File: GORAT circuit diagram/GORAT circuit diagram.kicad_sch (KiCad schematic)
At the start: 69 parts, among them J1 AudioJack2, J10 Conn_01x02_Socket, J11 Conn_01x02_Socket, J2 AudioJack2, J3 Conn_01x08_Socket, J4 Conn_01x08_Socket, J5 Conn_01x02_Socket, J6 Barrel_Jack, J7 Conn_01x02_Socket, J8 Conn_01x03_Socket, J9 Conn_01x03_Socket, Q1 J111, SW3 SW_Rotary4x3, SW8 SW_Rotary2x6, U1 OP07CP, U2 TL072ACP, U3 TL072ACP

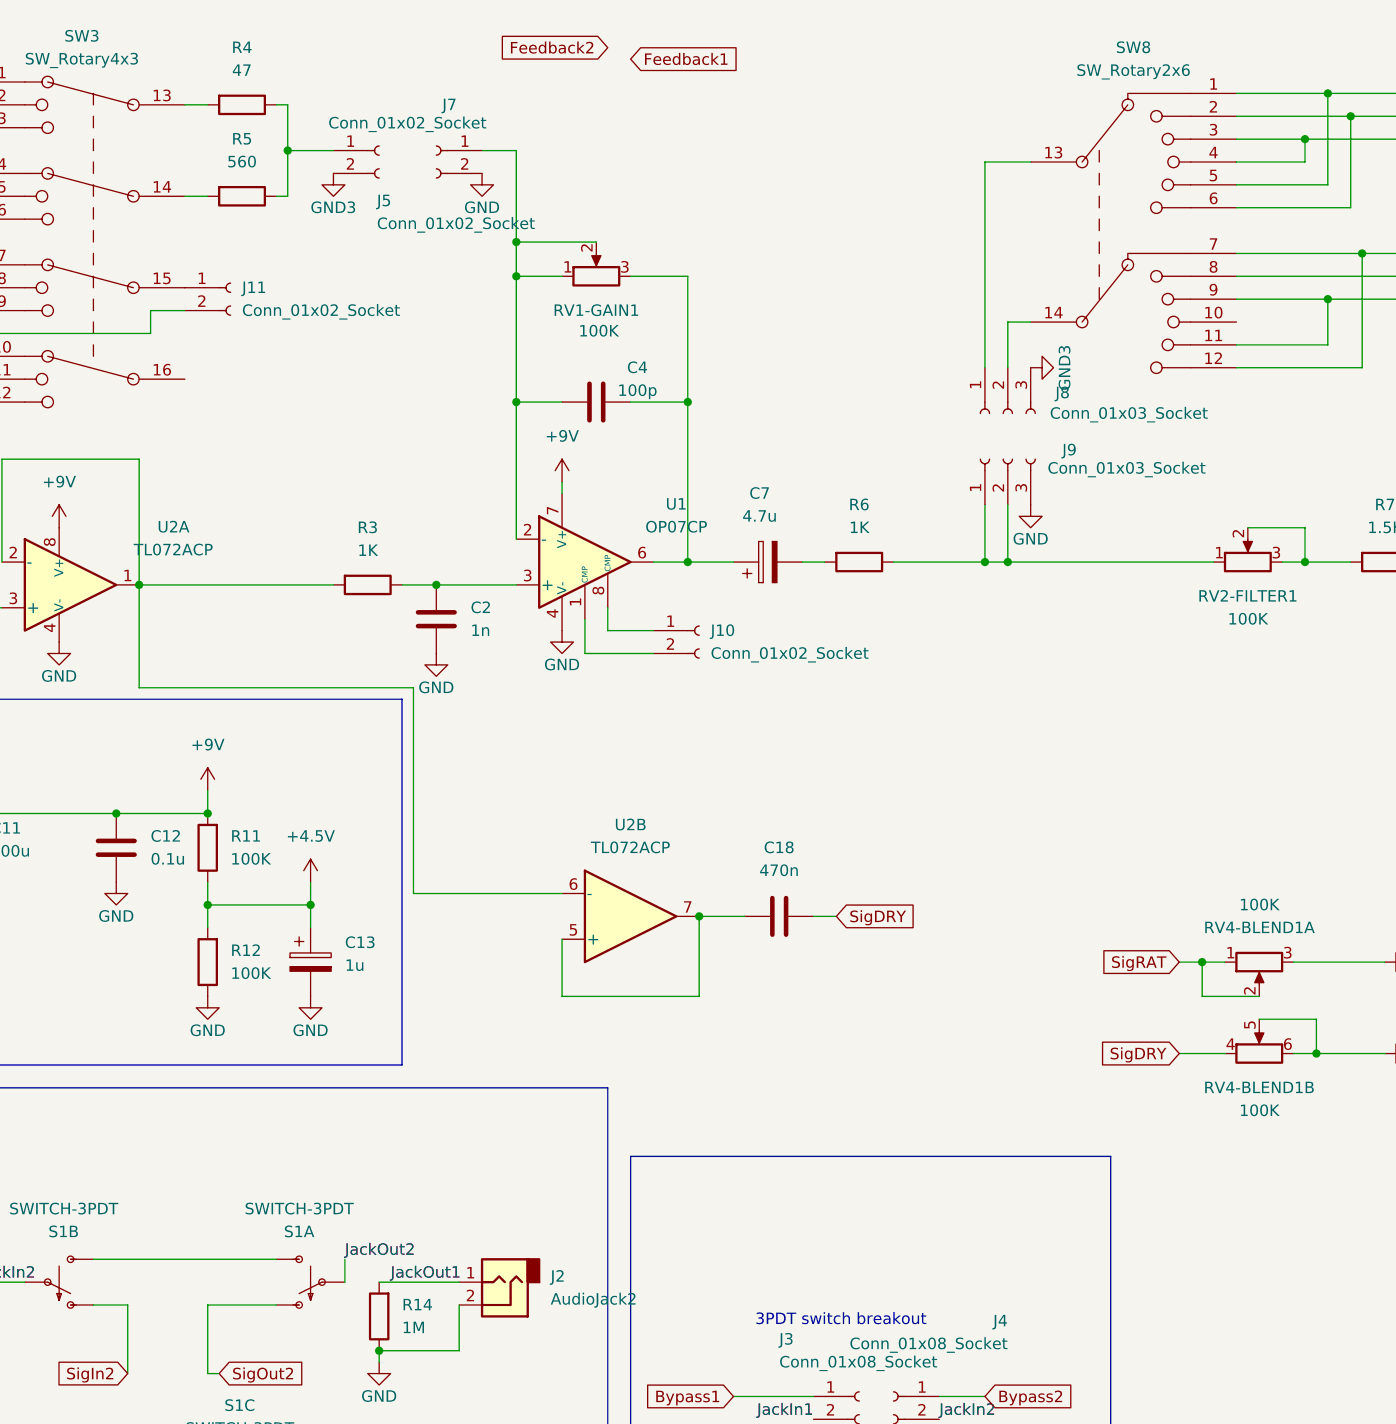
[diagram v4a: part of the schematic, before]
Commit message: Update KiCad PCB, add backups and artwork
Modify GORAT circuit diagram.kicad_pcb: reorder/renumber nets, adjust several pad/net assignments and component positions, and add numerous F.Fab properties (Availability, Check_prices, Description_1, MF, MP, Package, Price, Sim.Type, SnapEDA_Link) for multiple footprints. Remove several old backup ZIPs and add new timestamped backup ZIPs. Add new project assets: GoRAT.csv and artwork/renders (goram-mirror.svg, goram.png, goram.svg, underside.svg). These changes appear to be from a PCB/footprint update and exporting backup/artwork files.
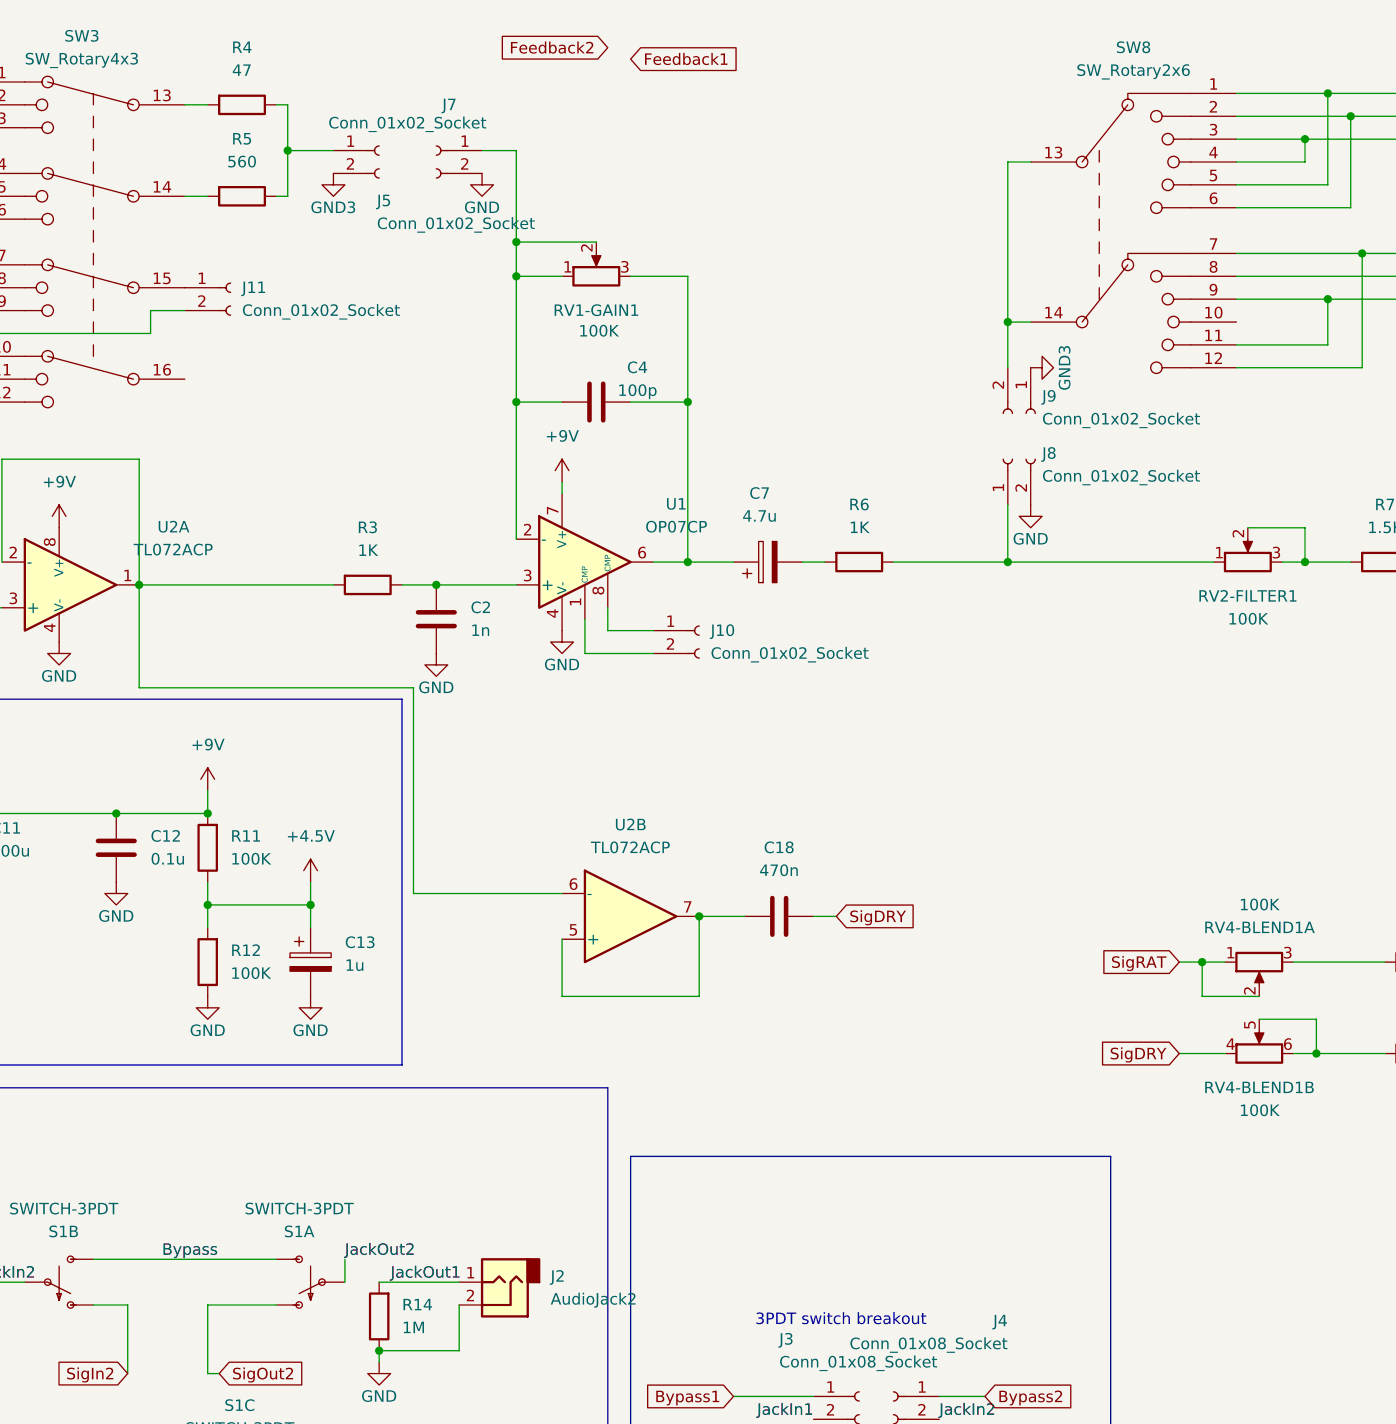
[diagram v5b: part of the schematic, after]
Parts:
- removed J8, J9: Conn_01x03_Socket, Connector_PinHeader_2.54mm:PinHeader_1x03_P2.54mm_Vertical, symbol Connector:Conn_01x03_Socket
- added J8, J9: Conn_01x02_Socket, Connector_PinHeader_2.54mm:PinHeader_1x02_P2.54mm_Vertical, symbol Connector:Conn_01x02_Socket
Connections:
- net GND: now also J8.2 (Pin_2)
- net GND3: now also J9.1 (Pin_1)
- net at SW8.13: now also SW8.14, J9.2 (Pin_2)
- net at R6.1, RV2-FILTER1.1: now also J8.1 (Pin_1)
- net Bypass: now reaches S1.P$3 (S), S1.P$6 (S)

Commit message: Update disc capacitor footprints and BOM
Replace THT disc capacitor footprints with smaller C_Disc_D4.7mm_W2.5mm variants across schematic and PCB (updated 3D model paths, silk/text positions, rotations and UUIDs). Update project metadata: change active board layer in .kicad_prl, set BOM export filename in .kicad_pro, and add generated BOM CSV/XLSX. Add KiCad backup archives and remove autosave/.lck temporary files to keep the repo clean.
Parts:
- C20, C21: footprint Capacitor_THT:C_Disc_D5.1mm_W3.2mm_P5.00mm -> Capacitor_THT:C_Disc_D4.7mm_W2.5mm_P5.00mm
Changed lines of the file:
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@@
 			)
 		)
-		(property "Footprint" "Capacitor_THT:C_Disc_D5.1mm_W3.2mm_P5.00mm"
+		(property "Footprint" "Capacitor_THT:C_Disc_D4.7mm_W2.5mm_P5.00mm"
 			(at 43.18 35.2552 0)
 			(effects
@@
 			)
 		)
-		(property "Footprint" "Capacitor_THT:C_Disc_D5.1mm_W3.2mm_P5.00mm"
+		(property "Footprint" "Capacitor_THT:C_Disc_D4.7mm_W2.5mm_P5.00mm"
 			(at 43.18 23.1648 0)
 			(effects

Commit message: BOM work
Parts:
- added TP1: Input, TestPoint:TestPoint_Pad_D2.0mm, symbol Connector:TestPoint
- added TP2: Pre-gain, TestPoint:TestPoint_Pad_D2.0mm, symbol Connector:TestPoint
- added TP3: Post-gain, TestPoint:TestPoint_Pad_D2.0mm, symbol Connector:TestPoint
- added TP4: Clipping, TestPoint:TestPoint_Pad_D2.0mm, symbol Connector:TestPoint
- added TP5: Dry, TestPoint:TestPoint_Pad_D2.0mm, symbol Connector:TestPoint
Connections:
- net SigDRY: now also TP5.1
- net at C4.1, C7.1, RV1-GAIN1.3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: now also TP3.1
- net at J8.1 (Pin_1), R6.1, RV2-FILTER1.1: now also TP4.1
- net at C2.2, R3.1, U1.3 (+): now also TP2.1
- net at C1.2, R2.1, U2.3 (+): now also TP1.1

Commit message: Fixed disconnection issue
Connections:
- net SigIn is gone; now on net SigIn1: C1.1
- net SigOut is gone; now on net SigOut1: C19.2
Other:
- note removed: "3PDT switch breakout"
- moved on the sheet: D4, J1, J2, J3, J4, J6, R1, R13, R14, S1A, S1B, S1C
